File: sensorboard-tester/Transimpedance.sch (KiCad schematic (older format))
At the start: 16 parts, among them J5 StabilizingCap, J7 Sensor, J8 PTVoltage, J9 PTCurrent, U2 LD1086V33-DG, U3 MIC5366-2.0YC5-TR

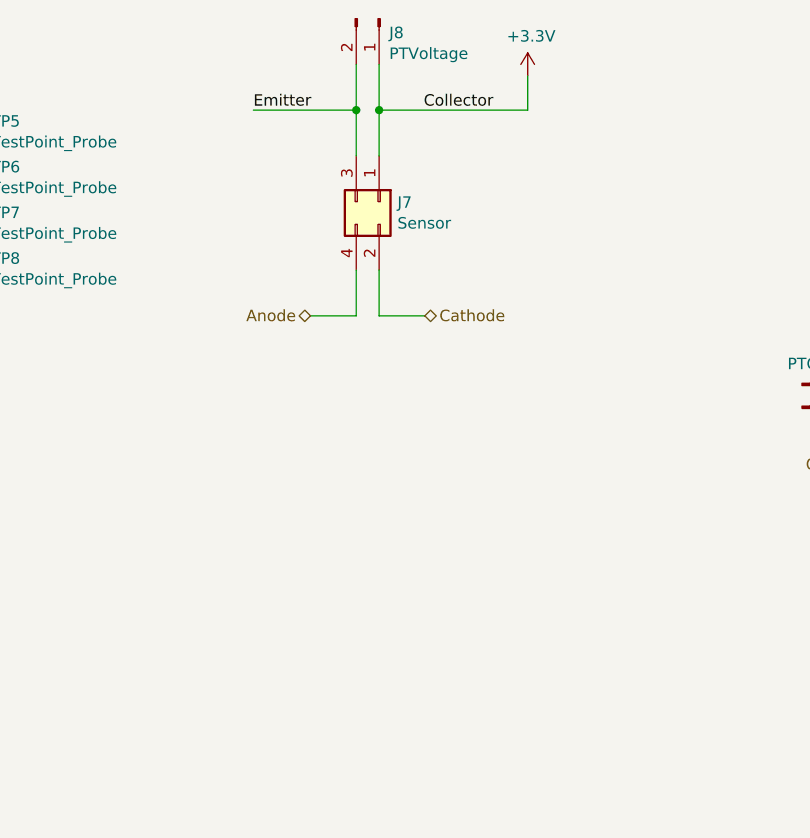
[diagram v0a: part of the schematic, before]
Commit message: Include mirrored headers for the sensorboards, in case their header has to be flipped.
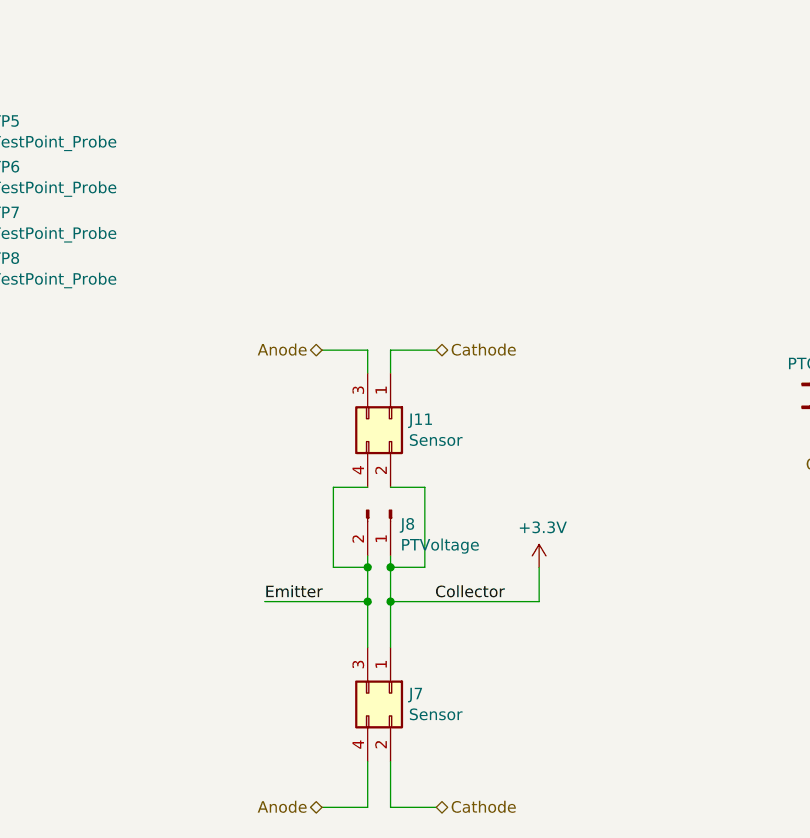
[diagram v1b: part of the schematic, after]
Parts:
- added J11: Sensor, Pin_Headers:Pin_Header_Straight_2x02_Pitch2.54mm, symbol Connector_Generic:Conn_02x02_Odd_Even
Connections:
- net +3V3: now also J11.2 (Pin_2)
- net Anode: now also J11.3 (Pin_3)
- net Cathode: now also J11.1 (Pin_1)
- net Emitter: now also J11.4 (Pin_4)
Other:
- moved on the sheet: J7, J8
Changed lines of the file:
@@
 L Connector_Generic:Conn_02x02_Odd_Even J?
 U 1 1 5FC69E13
-P 3550 1700
+P 3600 3850
 AR Path="/5FC34DE6/5FC69E13" Ref="J?"  Part="1"
 AR Path="/5FC566FE/5FC69E13" Ref="J7"  Part="1"
-F 0 "J7" V 3554 1780 50  0000 L CNN
-F 1 "Sensor" V 3645 1780 50  0000 L CNN
-F 2 "Pin_Headers:Pin_Header_Straight_2x02_Pitch2.54mm" H 3550 1700 50  0001 C CNN
-F 3 "~" H 3550 1700 50  0001 C CNN
-	1    3550 1700
+F 0 "J7" V 3604 3930 50  0000 L CNN
+F 1 "Sensor" V 3695 3930 50  0000 L CNN
+F 2 "Pin_Headers:Pin_Header_Straight_2x02_Pitch2.54mm" H 3600 3850 50  0001 C CNN
+F 3 "~" H 3600 3850 50  0001 C CNN
+	1    3600 3850
 	0    1    1    0
 $EndComp
 Wire Wire Line
-	3550 1500 3550 1300
-Wire Wire Line
-	3450 1500 3450 1300
-Wire Wire Line
-	3450 1300 3000 1300
-Wire Wire Line
-	3450 2000 3450 2200
-Wire Wire Line
-	3450 2200 3250 2200
-Wire Wire Line
-	3550 2000 3550 2200
-Wire Wire Line
-	3550 2200 3750 2200
-Text Label 3000 1300 0    50   ~ 0
+	3600 3650 3600 3450
+Wire Wire Line
+	3500 3650 3500 3450
+Wire Wire Line
+	3500 3450 3050 3450
+Wire Wire Line
+	3500 4150 3500 4350
+Wire Wire Line
+	3500 4350 3300 4350
+Wire Wire Line
+	3600 4150 3600 4350
+Wire Wire Line
+	3600 4350 3800 4350
+Text Label 3050 3450 0    50   ~ 0
 Emitter
-Text Label 4050 1300 2    50   ~ 0
+Text Label 4100 3450 2    50   ~ 0
 Collector
 $Comp
@@
 L Connector:Conn_01x02_Male J8
 U 1 1 5FC791F7
-P 3550 900
-F 0 "J8" V 3612 944 50  0000 L CNN
-F 1 "PTVoltage" V 3703 944 50  0000 L CNN
-F 2 "Pin_Headers:Pin_Header_Straight_1x02_Pitch2.54mm" H 3550 900 50  0001 C CNN
-F 3 "~" H 3550 900 50  0001 C CNN
-	1    3550 900
+P 3600 3050
+F 0 "J8" V 3662 3094 50  0000 L CNN
+F 1 "PTVoltage" V 3753 3094 50  0000 L CNN
+F 2 "Pin_Headers:Pin_Header_Straight_1x02_Pitch2.54mm" H 3600 3050 50  0001 C CNN
+F 3 "~" H 3600 3050 50  0001 C CNN
+	1    3600 3050
 	0    1    1    0
 $EndComp
 Wire Wire Line
-	3450 1300 3450 1100
-Connection ~ 3450 1300
-Wire Wire Line
-	3550 1300 3550 1100
-Connection ~ 3550 1300
-Text HLabel 3250 2200 0    50   BiDi ~ 0
+	3500 3450 3500 3300
+Connection ~ 3500 3450
+Wire Wire Line
+	3600 3450 3600 3300
+Connection ~ 3600 3450
+Text HLabel 3300 4350 0    50   BiDi ~ 0
 Anode
-Text HLabel 3750 2200 2    50   BiDi ~ 0
+Text HLabel 3800 4350 2    50   BiDi ~ 0
 Cathode
 Wire Wire Line
@@
 Emitter
 Wire Wire Line
-	4200 1300 4200 1150
-Wire Wire Line
-	3550 1300 4200 1300
+	4250 3450 4250 3300
+Wire Wire Line
+	3600 3450 4250 3450
 $Comp
 L power:+3.3V #PWR0111
 U 1 1 64677130
-P 4200 1150
-F 0 "#PWR0111" H 4200 1000 50  0001 C CNN
-F 1 "+3.3V" H 4215 1323 50  0000 C CNN
-F 2 "" H 4200 1150 50  0001 C CNN
-F 3 "" H 4200 1150 50  0001 C CNN
-	1    4200 1150
+P 4250 3300
+F 0 "#PWR0111" H 4250 3150 50  0001 C CNN
+F 1 "+3.3V" H 4265 3473 50  0000 C CNN
+F 2 "" H 4250 3300 50  0001 C CNN
+F 3 "" H 4250 3300 50  0001 C CNN
+	1    4250 3300
 	1    0    0    -1
 $EndComp
@@
 Wire Wire Line
 	6450 3150 6700 3150
+$Comp
+L Connector_Generic:Conn_02x02_Odd_Even J?
+U 1 1 5FE14A6D
+P 3600 2650
+AR Path="/5FC34DE6/5FE14A6D" Ref="J?"  Part="1"
+AR Path="/5FC566FE/5FE14A6D" Ref="J11"  Part="1"
+F 0 "J11" V 3604 2730 50  0000 L CNN
+F 1 "Sensor" V 3695 2730 50  0000 L CNN
+F 2 "Pin_Headers:Pin_Header_Straight_2x02_Pitch2.54mm" H 3600 2650 50  0001 C CNN
+F 3 "~" H 3600 2650 50  0001 C CNN
+	1    3600 2650
+	0    1    1    0
+$EndComp
+Wire Wire Line
+	3500 2950 3350 2950
+Wire Wire Line
+	3350 2950 3350 3300
+Wire Wire Line
+	3350 3300 3500 3300
+Connection ~ 3500 3300
+Wire Wire Line
+	3500 3300 3500 3250
+Wire Wire Line
+	3600 2950 3750 2950
+Wire Wire Line
+	3750 2950 3750 3300
+Wire Wire Line
+	3750 3300 3600 3300
+Connection ~ 3600 3300
+Wire Wire Line
+	3600 3300 3600 3250
+Wire Wire Line
+	3500 2450 3500 2350
+Wire Wire Line
+	3500 2350 3300 2350
+Wire Wire Line
+	3600 2450 3600 2350
+Wire Wire Line
+	3600 2350 3800 2350
+Text HLabel 3300 2350 0    50   BiDi ~ 0
+Anode
+Text HLabel 3800 2350 2    50   BiDi ~ 0
+Cathode
 $EndSCHEMATC

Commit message: Cleanup and reconcile the headers. Switch to SOT23 regulators for both.
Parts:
- removed J8: PTVoltage, Pin_Headers:Pin_Header_Straight_1x02_Pitch2.54mm, symbol Connector:Conn_01x02_Male
- removed U3: MIC5366-2.0YC5-TR, TO_SOT_Packages_SMD:SOT-353_SC-70-5_Handsoldering, symbol Regulator_Linear:MIC5365-3.3YC5
- added U3: MCP1700T-2002E/TT, TO_SOT_Packages_SMD:SOT-23, symbol Regulator_Linear:AMS1117-1.5
- J5: symbol Connector:Conn_01x02_Male -> Connector:Conn_01x02_Female
- J9: value PTCurrent -> PTCurrentShunt
- U2: value LD1086V33-DG -> AP2120N-3.3TRG1; footprint TO_SOT_Packages_THT:TO-220-3_Vertical -> TO_SOT_Packages_SMD:SOT-23
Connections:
- net +5V: now also U3.3 (VI)
- net GND: now also U3.1 (GND)
- net OP+: now also U3.2 (VO)
- net OP-: now also J5.2 (Pin_2); no longer J5.1 (Pin_1)
- net OP_OUT: now also J5.1 (Pin_1); no longer J5.2 (Pin_2)
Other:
- moved on the sheet: C2, C3, C4, C5, J11, J7, J9, RV3, TP10, U2
